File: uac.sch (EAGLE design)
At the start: 158 parts, among them Q1 2N7002CK4SST

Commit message: Arcdozen 2 toegevoegd
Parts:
- added Q2: 2N7002CK4SST, Custom components:2N7002CK4SST
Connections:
- new net ARCDOZEN_2: Q2.G
- new net N$1: HOUR1.C, MIN5.C, MIN6.C, MIN7.C, MIN8.C, MIN9.C, Q2.D, SEC5.C, SEC6.C, SEC7.C, SEC8.C, SEC9.C, SPECIAL1.C
- net DOZEN1: now also HOUR1.A
- net DOZEN10: now also SEC8.A
- net DOZEN11: now also SEC9.A
- net DOZEN12: now also SPECIAL1.A
- net DOZEN2: now also MIN5.A
- net DOZEN3: now also MIN6.A
- net DOZEN4: now also MIN7.A
- net DOZEN5: now also MIN8.A
- net DOZEN6: now also MIN9.A
- net DOZEN7: now also SEC5.A
- net DOZEN8: now also SEC6.A
- net DOZEN9: now also SEC7.A
- net GND: now also Q2.S
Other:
- moved on the sheet: HOUR1, MIN5, MIN6, MIN7, MIN8, MIN9, SEC5, SEC6, SEC7, SEC8, SEC9, SPECIAL1

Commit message: Leds aangesloten
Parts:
- added Q10, Q11, Q12, Q3, Q4, Q5, Q6, Q7, Q8, Q9: 2N7002CK4SST, Custom components:2N7002CK4SST
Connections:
- new net ARCDOZEN_10: Q10.G
- new net ARCDOZEN_11: Q11.G
- new net ARCDOZEN_12: Q12.G
- new net ARCDOZEN_3: Q3.G
- new net ARCDOZEN_4: Q4.G
- new net ARCDOZEN_5: Q5.G
- new net ARCDOZEN_6: Q6.G
- new net ARCDOZEN_7: Q7.G
- new net ARCDOZEN_8: Q8.G
- new net ARCDOZEN_9: Q9.G
- new net N$10: HOUR9.C, MIN45.C, MIN46.C, MIN47.C, MIN48.C, MIN49.C, Q10.D, SEC45.C, SEC46.C, SEC47.C, SEC48.C, SEC49.C, SPECIAL9.C
- new net N$11: HOUR10.C, MIN50.C, MIN51.C, MIN52.C, MIN53.C, MIN54.C, Q11.D, SEC50.C, SEC51.C, SEC52.C, SEC53.C, SEC54.C, SPECIAL10.C
- new net N$12: HOUR11.C, MIN55.C, MIN56.C, MIN57.C, MIN58.C, MIN59.C, Q12.D, SEC55.C, SEC56.C, SEC57.C, SEC58.C, SEC59.C, SPECIAL11.C
- new net N$2: HOUR2.C, MIN10.C, MIN11.C, MIN12.C, MIN13.C, MIN14.C, Q3.D, SEC10.C, SEC11.C, SEC12.C, SEC13.C, SEC14.C, SPECIAL2.C
- new net N$4: HOUR3.C, MIN15.C, MIN16.C, MIN17.C, MIN18.C, MIN19.C, Q4.D, SEC15.C, SEC16.C, SEC17.C, SEC18.C, SEC19.C, SPECIAL3.C
- new net N$5: HOUR4.C, MIN20.C, MIN21.C, MIN22.C, MIN23.C, MIN24.C, Q5.D, SEC20.C, SEC21.C, SEC22.C, SEC23.C, SEC24.C, SPECIAL4.C
- new net N$6: HOUR5.C, MIN25.C, MIN26.C, MIN27.C, MIN28.C, MIN29.C, Q6.D, SEC25.C, SEC26.C, SEC27.C, SEC28.C, SEC29.C, SPECIAL5.C
- new net N$7: HOUR6.C, MIN30.C, MIN31.C, MIN32.C, MIN33.C, MIN34.C, Q7.D, SEC30.C, SEC31.C, SEC32.C, SEC33.C, SEC34.C, SPECIAL6.C
- new net N$8: HOUR7.C, MIN35.C, MIN36.C, MIN37.C, MIN38.C, MIN39.C, Q8.D, SEC35.C, SEC36.C, SEC37.C, SEC38.C, SEC39.C, SPECIAL7.C
- new net N$9: HOUR8.C, MIN40.C, MIN41.C, MIN42.C, MIN43.C, MIN44.C, Q9.D, SEC40.C, SEC41.C, SEC42.C, SEC43.C, SEC44.C, SPECIAL8.C
- net DOZEN1: now also HOUR10.A, HOUR11.A, HOUR2.A, HOUR3.A, HOUR4.A, HOUR5.A, HOUR6.A, HOUR7.A, HOUR8.A, HOUR9.A
- net DOZEN10: now also SEC13.A, SEC18.A, SEC23.A, SEC28.A, SEC33.A, SEC38.A, SEC43.A, SEC48.A, SEC53.A, SEC58.A
- net DOZEN11: now also SEC14.A, SEC19.A, SEC24.A, SEC29.A, SEC34.A, SEC39.A, SEC44.A, SEC49.A, SEC54.A, SEC59.A
- net DOZEN12: now also SPECIAL10.A, SPECIAL11.A, SPECIAL2.A, SPECIAL3.A, SPECIAL4.A, SPECIAL5.A, SPECIAL6.A, SPECIAL7.A, SPECIAL8.A, SPECIAL9.A
- net DOZEN2: now also MIN10.A, MIN15.A, MIN20.A, MIN25.A, MIN30.A, MIN35.A, MIN40.A, MIN45.A, MIN50.A, MIN55.A
- net DOZEN3: now also MIN11.A, MIN16.A, MIN21.A, MIN26.A, MIN31.A, MIN36.A, MIN41.A, MIN46.A, MIN51.A, MIN56.A
- net DOZEN4: now also MIN12.A, MIN17.A, MIN22.A, MIN27.A, MIN32.A, MIN37.A, MIN42.A, MIN47.A, MIN52.A, MIN57.A
- net DOZEN5: now also MIN13.A, MIN18.A, MIN23.A, MIN28.A, MIN33.A, MIN38.A, MIN43.A, MIN48.A, MIN53.A, MIN58.A
- net DOZEN6: now also MIN14.A, MIN19.A, MIN24.A, MIN29.A, MIN34.A, MIN39.A, MIN44.A, MIN49.A, MIN54.A, MIN59.A
- net DOZEN7: now also SEC10.A, SEC15.A, SEC20.A, SEC25.A, SEC30.A, SEC35.A, SEC40.A, SEC45.A, SEC50.A, SEC55.A
- net DOZEN8: now also SEC11.A, SEC16.A, SEC21.A, SEC26.A, SEC31.A, SEC36.A, SEC41.A, SEC46.A, SEC51.A, SEC56.A
- net DOZEN9: now also SEC12.A, SEC17.A, SEC22.A, SEC27.A, SEC32.A, SEC37.A, SEC42.A, SEC47.A, SEC52.A, SEC57.A
- net GND: now also Q10.S, Q11.S, Q12.S, Q3.S, Q4.S, Q5.S, Q6.S, Q7.S, Q8.S, Q9.S
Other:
- moved on the sheet: HOUR0, HOUR1, HOUR10, HOUR11, HOUR2, HOUR3, HOUR4, HOUR5, HOUR6, HOUR7, HOUR8, HOUR9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

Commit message: 64 pin Micro geplaatst
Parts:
- removed Q1, Q10, Q11, Q12, Q2, Q3, Q4, Q5, Q6, Q7, Q8, Q9: 2N7002CK4SST, Custom components:2N7002CK4SST
- added C1, C2, C3, C4: 100n, Custom components:C-EUC0603
- added Y1: RESONATORSMD, Custom components:RESONATORSMD
- U$1: value (none) -> STM32F103CBT6; device stm32_lqfp144:STM32F103ZE -> stm32:STM32F103CBT6
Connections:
- removed net ARCDOZEN_2: Q2.G
- removed net N$10: HOUR9.C, MIN45.C, MIN46.C, MIN47.C, MIN48.C, MIN49.C, Q10.D, SEC45.C, SEC46.C, SEC47.C, SEC48.C, SEC49.C, SPECIAL9.C
- removed net N$11: HOUR10.C, MIN50.C, MIN51.C, MIN52.C, MIN53.C, MIN54.C, Q11.D, SEC50.C, SEC51.C, SEC52.C, SEC53.C, SEC54.C, SPECIAL10.C
- removed net N$12: HOUR11.C, MIN55.C, MIN56.C, MIN57.C, MIN58.C, MIN59.C, Q12.D, SEC55.C, SEC56.C, SEC57.C, SEC58.C, SEC59.C, SPECIAL11.C
- removed net N$3: HOUR0.C, MIN0.C, MIN1.C, MIN2.C, MIN3.C, MIN4.C, Q1.D, SEC0.C, SEC1.C, SEC2.C, SEC3.C, SEC4.C, SPECIAL0.C
- removed net N$4: HOUR3.C, MIN15.C, MIN16.C, MIN17.C, MIN18.C, MIN19.C, Q4.D, SEC15.C, SEC16.C, SEC17.C, SEC18.C, SEC19.C, SPECIAL3.C
- removed net N$5: HOUR4.C, MIN20.C, MIN21.C, MIN22.C, MIN23.C, MIN24.C, Q5.D, SEC20.C, SEC21.C, SEC22.C, SEC23.C, SEC24.C, SPECIAL4.C
- removed net N$6: HOUR5.C, MIN25.C, MIN26.C, MIN27.C, MIN28.C, MIN29.C, Q6.D, SEC25.C, SEC26.C, SEC27.C, SEC28.C, SEC29.C, SPECIAL5.C
- removed net N$7: HOUR6.C, MIN30.C, MIN31.C, MIN32.C, MIN33.C, MIN34.C, Q7.D, SEC30.C, SEC31.C, SEC32.C, SEC33.C, SEC34.C, SPECIAL6.C
- removed net N$8: HOUR7.C, MIN35.C, MIN36.C, MIN37.C, MIN38.C, MIN39.C, Q8.D, SEC35.C, SEC36.C, SEC37.C, SEC38.C, SEC39.C, SPECIAL7.C
- removed net N$9: HOUR8.C, MIN40.C, MIN41.C, MIN42.C, MIN43.C, MIN44.C, Q9.D, SEC40.C, SEC41.C, SEC42.C, SEC43.C, SEC44.C, SPECIAL8.C
- new net +3V3: C1.2, C2.2, C3.2, C4.2, U$1.VBAT, U$1.VDD_1, U$1.VDD_2, U$1.VDD_3, U$1.VDD_4, U$1.VDD_A
- net ARCDOZEN_1: now also HOUR0.C, MIN0.C, MIN1.C, MIN2.C, MIN3.C, MIN4.C, SEC0.C, SEC1.C, SEC2.C, SEC3.C, SEC4.C, SPECIAL0.C; no longer Q1.G
- net ARCDOZEN_10: now also HOUR9.C, MIN45.C, MIN46.C, MIN47.C, MIN48.C, MIN49.C, SEC45.C, SEC46.C, SEC47.C, SEC48.C, SEC49.C, SPECIAL9.C; no longer Q10.G
- net ARCDOZEN_11: now also HOUR10.C, MIN50.C, MIN51.C, MIN52.C, MIN53.C, MIN54.C, SEC50.C, SEC51.C, SEC52.C, SEC53.C, SEC54.C, SPECIAL10.C; no longer Q11.G
- net ARCDOZEN_12: now also HOUR11.C, MIN55.C, MIN56.C, MIN57.C, MIN58.C, MIN59.C, SEC55.C, SEC56.C, SEC57.C, SEC58.C, SEC59.C, SPECIAL11.C; no longer Q12.G
- net ARCDOZEN_3: now also HOUR1.C, HOUR2.C, MIN10.C, MIN11.C, MIN12.C, MIN13.C, MIN14.C, MIN5.C, MIN6.C, MIN7.C, MIN8.C, MIN9.C, SEC10.C, SEC11.C, SEC12.C, SEC13.C, SEC14.C, SEC5.C, SEC6.C, SEC7.C, SEC8.C, SEC9.C, SPECIAL1.C, SPECIAL2.C; no longer Q3.G
- net ARCDOZEN_4: now also HOUR3.C, MIN15.C, MIN16.C, MIN17.C, MIN18.C, MIN19.C, SEC15.C, SEC16.C, SEC17.C, SEC18.C, SEC19.C, SPECIAL3.C; no longer Q4.G
- net ARCDOZEN_5: now also HOUR4.C, MIN20.C, MIN21.C, MIN22.C, MIN23.C, MIN24.C, SEC20.C, SEC21.C, SEC22.C, SEC23.C, SEC24.C, SPECIAL4.C; no longer Q5.G
- net ARCDOZEN_6: now also HOUR5.C, MIN25.C, MIN26.C, MIN27.C, MIN28.C, MIN29.C, SEC25.C, SEC26.C, SEC27.C, SEC28.C, SEC29.C, SPECIAL5.C; no longer Q6.G
- net ARCDOZEN_7: now also HOUR6.C, MIN30.C, MIN31.C, MIN32.C, MIN33.C, MIN34.C, SEC30.C, SEC31.C, SEC32.C, SEC33.C, SEC34.C, SPECIAL6.C; no longer Q7.G
- net ARCDOZEN_8: now also HOUR7.C, MIN35.C, MIN36.C, MIN37.C, MIN38.C, MIN39.C, SEC35.C, SEC36.C, SEC37.C, SEC38.C, SEC39.C, SPECIAL7.C; no longer Q8.G
- net ARCDOZEN_9: now also HOUR8.C, MIN40.C, MIN41.C, MIN42.C, MIN43.C, MIN44.C, SEC40.C, SEC41.C, SEC42.C, SEC43.C, SEC44.C, SPECIAL8.C; no longer Q9.G
- net GND: now also C1.1, C2.1, C3.1, C4.1, U$1.VSS_1, U$1.VSS_2, U$1.VSS_3, U$1.VSS_4, U$1.VSS_A, Y1.2; no longer Q1.S, Q10.S, Q11.S, Q12.S, Q2.S, Q3.S, Q4.S, Q5.S, Q6.S, Q7.S, Q8.S, Q9.S
- net N$1: now also U$1.PD1-OSC_OUT, Y1.3; no longer HOUR1.C, MIN5.C, MIN6.C, MIN7.C, MIN8.C, MIN9.C, Q2.D, SEC5.C, SEC6.C, SEC7.C, SEC8.C, SEC9.C, SPECIAL1.C
- net N$2: now also U$1.PD0-OSC_IN, Y1.1; no longer HOUR2.C, MIN10.C, MIN11.C, MIN12.C, MIN13.C, MIN14.C, Q3.D, SEC10.C, SEC11.C, SEC12.C, SEC13.C, SEC14.C, SPECIAL2.C

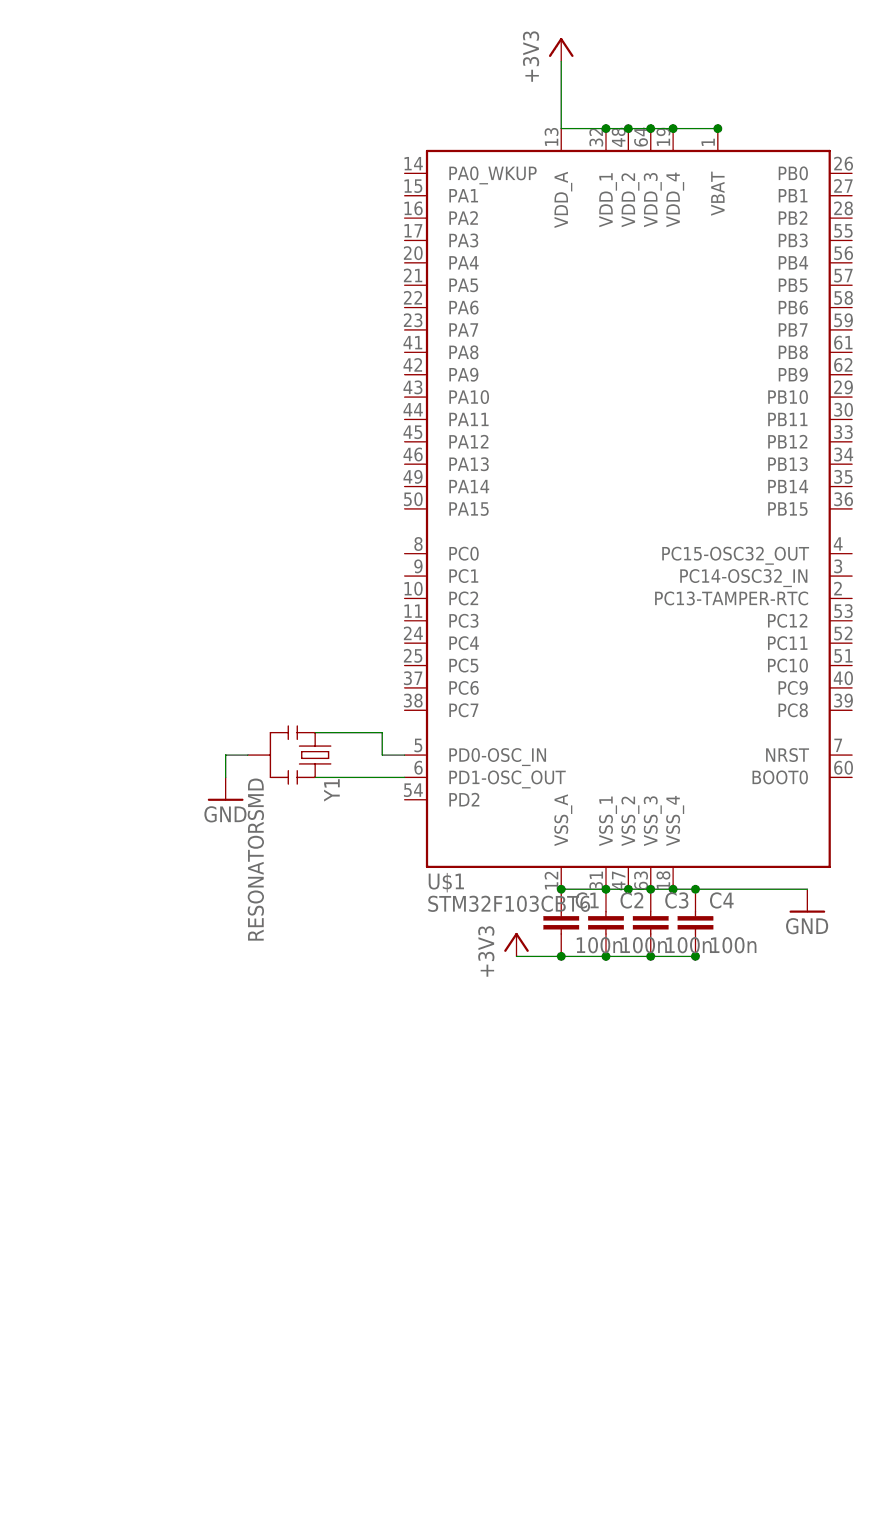
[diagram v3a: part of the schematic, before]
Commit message: condensatoren
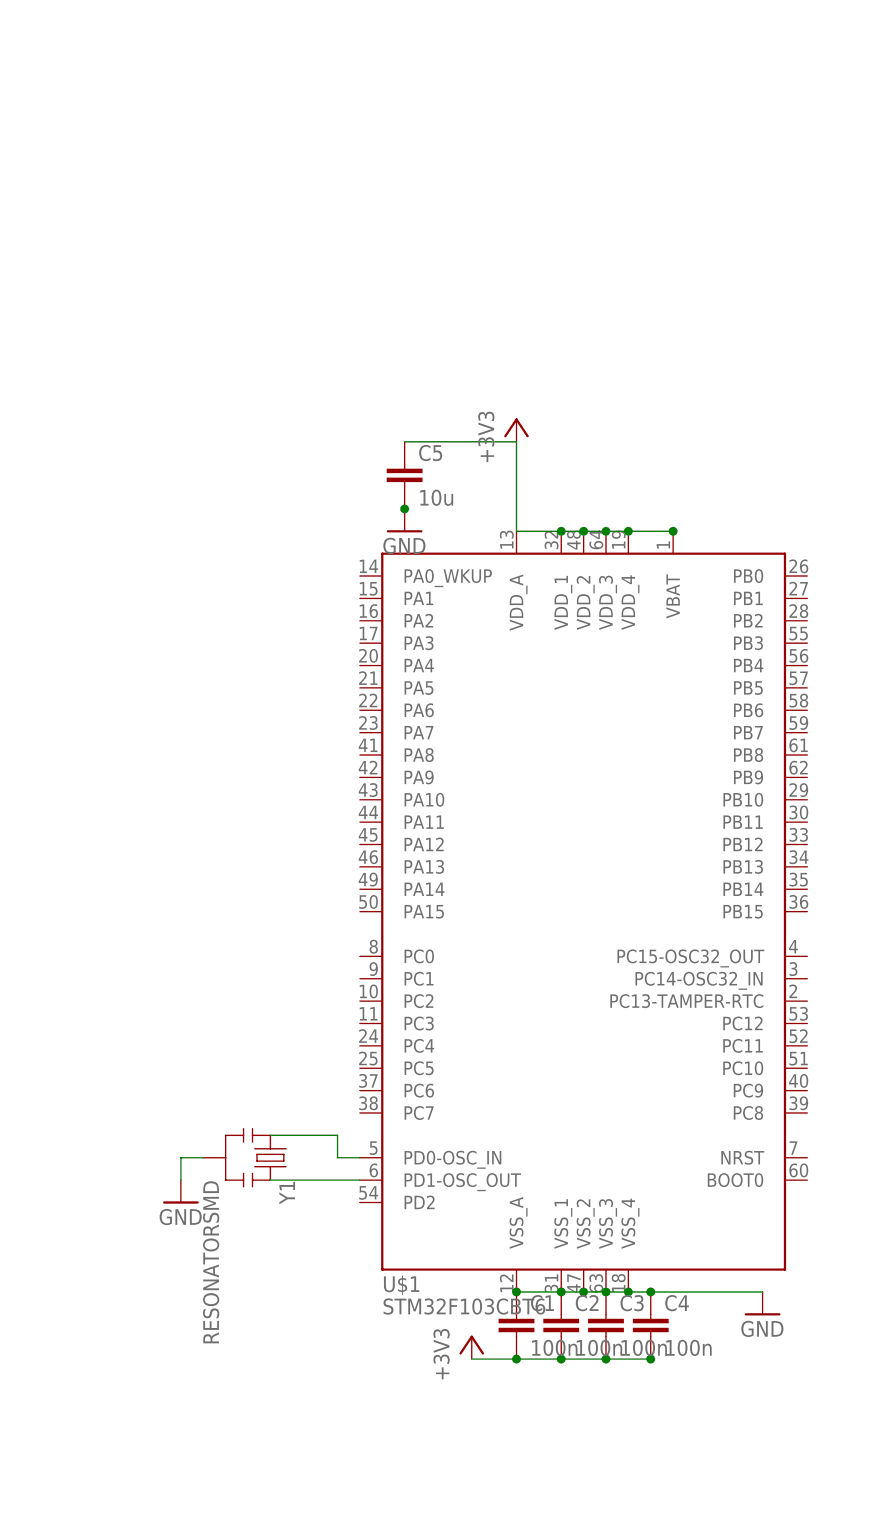
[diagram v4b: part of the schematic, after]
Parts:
- added C5: 10u, Custom components:C-EUC0603
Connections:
- net +3V3: now also C5.1
- net GND: now also C5.2
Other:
- moved on the sheet: C1, C2, C3, C4, U$1, Y1
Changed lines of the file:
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@@
 <part name="Y1" library="Custom components" deviceset="RESONATOR" device="SMD"/>
 <part name="GND2" library="Custom components" deviceset="GND" device=""/>
+<part name="C5" library="Custom components" deviceset="C-EU" device="C0603" value="10u"/>
+<part name="GND3" library="Custom components" deviceset="GND" device=""/>
 </parts>
 <sheets>
@@
 <instance part="R11" gate="G$1" x="48.26" y="304.8" rot="R180"/>
 <instance part="R12" gate="G$1" x="48.26" y="297.18" rot="R180"/>
-<instance part="U$1" gate="G$1" x="635" y="393.7"/>
-<instance part="GND1" gate="1" x="668.02" y="332.74"/>
-<instance part="+3V1" gate="G$1" x="640.08" y="431.8"/>
-<instance part="C1" gate="G$1" x="640.08" y="332.74"/>
-<instance part="C2" gate="G$1" x="645.16" y="332.74"/>
-<instance part="C3" gate="G$1" x="650.24" y="332.74"/>
-<instance part="C4" gate="G$1" x="655.32" y="332.74"/>
-<instance part="+3V2" gate="G$1" x="635" y="330.2"/>
-<instance part="Y1" gate="G$1" x="612.14" y="350.52" rot="R270"/>
-<instance part="GND2" gate="1" x="601.98" y="345.44"/>
+<instance part="U$1" gate="G$1" x="629.92" y="347.98"/>
+<instance part="GND1" gate="1" x="662.94" y="287.02"/>
+<instance part="+3V1" gate="G$1" x="635" y="388.62"/>
+<instance part="C1" gate="G$1" x="635" y="287.02"/>
+<instance part="C2" gate="G$1" x="640.08" y="287.02"/>
+<instance part="C3" gate="G$1" x="645.16" y="287.02"/>
+<instance part="C4" gate="G$1" x="650.24" y="287.02"/>
+<instance part="+3V2" gate="G$1" x="629.92" y="284.48"/>
+<instance part="Y1" gate="G$1" x="607.06" y="304.8" rot="R270"/>
+<instance part="GND2" gate="1" x="596.9" y="299.72"/>
+<instance part="C5" gate="G$1" x="622.3" y="383.54"/>
+<instance part="GND3" gate="1" x="622.3" y="375.92"/>
 </instances>
 <busses>
@@
 <pinref part="U$1" gate="G$1" pin="VSS_A"/>
 <pinref part="U$1" gate="G$1" pin="VSS_1"/>
-<wire x1="640.08" y1="335.28" x2="645.16" y2="335.28" width="0.1524" layer="91"/>
+<wire x1="635" y1="289.56" x2="640.08" y2="289.56" width="0.1524" layer="91"/>
 <pinref part="U$1" gate="G$1" pin="VSS_2"/>
-<wire x1="645.16" y1="335.28" x2="647.7" y2="335.28" width="0.1524" layer="91"/>
+<wire x1="640.08" y1="289.56" x2="642.62" y2="289.56" width="0.1524" layer="91"/>
 <pinref part="U$1" gate="G$1" pin="VSS_3"/>
 <pinref part="U$1" gate="G$1" pin="VSS_4"/>
 <pinref part="GND1" gate="1" pin="GND"/>
-<wire x1="655.32" y1="335.28" x2="668.02" y2="335.28" width="0.1524" layer="91"/>
-<junction x="655.32" y="335.28"/>
-<junction x="650.24" y="335.28"/>
-<junction x="645.16" y="335.28"/>
-<junction x="640.08" y="335.28"/>
+<wire x1="650.24" y1="289.56" x2="662.94" y2="289.56" width="0.1524" layer="91"/>
+<junction x="650.24" y="289.56"/>
+<junction x="645.16" y="289.56"/>
+<junction x="640.08" y="289.56"/>
+<junction x="635" y="289.56"/>
 <pinref part="C1" gate="G$1" pin="1"/>
 <pinref part="C2" gate="G$1" pin="1"/>
 <pinref part="C3" gate="G$1" pin="1"/>
 <pinref part="C4" gate="G$1" pin="1"/>
-<wire x1="652.78" y1="335.28" x2="650.24" y2="335.28" width="0.1524" layer="91"/>
-<wire x1="655.32" y1="335.28" x2="652.78" y2="335.28" width="0.1524" layer="91"/>
-<wire x1="650.24" y1="335.28" x2="647.7" y2="335.28" width="0.1524" layer="91"/>
-<junction x="647.7" y="335.28"/>
-<junction x="652.78" y="335.28"/>
+<wire x1="647.7" y1="289.56" x2="645.16" y2="289.56" width="0.1524" layer="91"/>
+<wire x1="650.24" y1="289.56" x2="647.7" y2="289.56" width="0.1524" layer="91"/>
+<wire x1="645.16" y1="289.56" x2="642.62" y2="289.56" width="0.1524" layer="91"/>
+<junction x="642.62" y="289.56"/>
+<junction x="647.7" y="289.56"/>
 </segment>
 <segment>
 <pinref part="Y1" gate="G$1" pin="2"/>
 <pinref part="GND2" gate="1" pin="GND"/>
-<wire x1="604.52" y1="350.52" x2="601.98" y2="350.52" width="0.1524" layer="91"/>
-<wire x1="601.98" y1="350.52" x2="601.98" y2="347.98" width="0.1524" layer="91"/>
+<wire x1="599.44" y1="304.8" x2="596.9" y2="304.8" width="0.1524" layer="91"/>
+<wire x1="596.9" y1="304.8" x2="596.9" y2="302.26" width="0.1524" layer="91"/>
+</segment>
+<segment>
+<pinref part="C5" gate="G$1" pin="2"/>
+<pinref part="GND3" gate="1" pin="GND"/>
+<junction x="622.3" y="378.46"/>
 </segment>
 </net>
@@
 <pinref part="U$1" gate="G$1" pin="VBAT"/>
 <pinref part="U$1" gate="G$1" pin="VDD_4"/>
-<wire x1="657.86" y1="421.64" x2="652.78" y2="421.64" width="0.1524" layer="91"/>
+<wire x1="652.78" y1="375.92" x2="647.7" y2="375.92" width="0.1524" layer="91"/>
 <pinref part="U$1" gate="G$1" pin="VDD_3"/>
-<wire x1="652.78" y1="421.64" x2="650.24" y2="421.64" width="0.1524" layer="91"/>
+<wire x1="647.7" y1="375.92" x2="645.16" y2="375.92" width="0.1524" layer="91"/>
 <pinref part="U$1" gate="G$1" pin="VDD_2"/>
-<wire x1="650.24" y1="421.64" x2="647.7" y2="421.64" width="0.1524" layer="91"/>
+<wire x1="645.16" y1="375.92" x2="642.62" y2="375.92" width="0.1524" layer="91"/>
 <pinref part="U$1" gate="G$1" pin="VDD_1"/>
-<wire x1="647.7" y1="421.64" x2="645.16" y2="421.64" width="0.1524" layer="91"/>
+<wire x1="642.62" y1="375.92" x2="640.08" y2="375.92" width="0.1524" layer="91"/>
 <pinref part="U$1" gate="G$1" pin="VDD_A"/>
-<wire x1="645.16" y1="421.64" x2="640.08" y2="421.64" width="0.1524" layer="91"/>
+<wire x1="640.08" y1="375.92" x2="635" y2="375.92" width="0.1524" layer="91"/>
 <pinref part="+3V1" gate="G$1" pin="+3V3"/>
-<wire x1="640.08" y1="421.64" x2="640.08" y2="429.26" width="0.1524" layer="91"/>
-<junction x="645.16" y="421.64"/>
-<junction x="647.7" y="421.64"/>
-<junction x="650.24" y="421.64"/>
-<junction x="652.78" y="421.64"/>
-<junction x="657.86" y="421.64"/>
+<wire x1="635" y1="375.92" x2="635" y2="386.08" width="0.1524" layer="91"/>
+<junction x="640.08" y="375.92"/>
+<junction x="642.62" y="375.92"/>
+<junction x="645.16" y="375.92"/>
+<junction x="647.7" y="375.92"/>
+<junction x="652.78" y="375.92"/>
+<pinref part="C5" gate="G$1" pin="1"/>
+<wire x1="635" y1="386.08" x2="622.3" y2="386.08" width="0.1524" layer="91"/>
 </segment>
 <segment>
 <pinref part="C4" gate="G$1" pin="2"/>
 <pinref part="C3" gate="G$1" pin="2"/>
-<wire x1="655.32" y1="327.66" x2="650.24" y2="327.66" width="0.1524" layer="91"/>
+<wire x1="650.24" y1="281.94" x2="645.16" y2="281.94" width="0.1524" layer="91"/>
 <pinref part="C2" gate="G$1" pin="2"/>
-<wire x1="650.24" y1="327.66" x2="645.16" y2="327.66" width="0.1524" layer="91"/>
+<wire x1="645.16" y1="281.94" x2="640.08" y2="281.94" width="0.1524" layer="91"/>
 <pinref part="C1" gate="G$1" pin="2"/>
-<wire x1="645.16" y1="327.66" x2="640.08" y2="327.66" width="0.1524" layer="91"/>
+<wire x1="640.08" y1="281.94" x2="635" y2="281.94" width="0.1524" layer="91"/>
 <pinref part="+3V2" gate="G$1" pin="+3V3"/>
-<wire x1="640.08" y1="327.66" x2="635" y2="327.66" width="0.1524" layer="91"/>
-<junction x="640.08" y="327.66"/>
-<junction x="645.16" y="327.66"/>
-<junction x="650.24" y="327.66"/>
-<junction x="655.32" y="327.66"/>
+<wire x1="635" y1="281.94" x2="629.92" y2="281.94" width="0.1524" layer="91"/>
+<junction x="635" y="281.94"/>
+<junction x="640.08" y="281.94"/>
+<junction x="645.16" y="281.94"/>
+<junction x="650.24" y="281.94"/>
 </segment>
 </net>
@@
 <pinref part="U$1" gate="G$1" pin="PD1-OSC_OUT"/>
 <pinref part="Y1" gate="G$1" pin="3"/>
-<wire x1="622.3" y1="347.98" x2="612.14" y2="347.98" width="0.1524" layer="91"/>
+<wire x1="617.22" y1="302.26" x2="607.06" y2="302.26" width="0.1524" layer="91"/>
 </segment>
 </net>
@@
 <segment>
 <pinref part="U$1" gate="G$1" pin="PD0-OSC_IN"/>
-<wire x1="622.3" y1="350.52" x2="619.76" y2="350.52" width="0.1524" layer="91"/>
-<wire x1="619.76" y1="350.52" x2="619.76" y2="353.06" width="0.1524" layer="91"/>
+<wire x1="617.22" y1="304.8" x2="614.68" y2="304.8" width="0.1524" layer="91"/>
+<wire x1="614.68" y1="304.8" x2="614.68" y2="307.34" width="0.1524" layer="91"/>
 <pinref part="Y1" gate="G$1" pin="1"/>
-<wire x1="619.76" y1="353.06" x2="612.14" y2="353.06" width="0.1524" layer="91"/>
-</segment>
-</net>
+<wire x1="614.68" y1="307.34" x2="607.06" y2="307.34" width="0.1524" layer="91"/>
+</segment>
+</net>
